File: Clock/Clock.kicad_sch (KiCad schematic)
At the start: 65 parts, among them J1 Conn buss, J10 Conn_buss, J11 Conn_buss, J12 Conn_buss, J13 Register_A-1,2 LED Conn, J14 Register_B-1,2 LED Conn, J15 Program Counter LED Conn, J16 Memory Address Reg LED Conn, J17 Instruction Reg LED Conn, J18 Conn_01x02_Pin, J19 Conn_02x04_Top_Bottom, J2 USB4125-GF-A, J3 Fuse-Block, J4 Conn buss, J5 Conn_buss, J6 Conn_buss, J7 Conn_buss, J8 Conn_buss, J9 Conn_buss, SW1 SW_CLK_mono, SW2 SW_Select_Mon/Ast, SW3 SW_SPST, SW4 SW_Select_Oscilator, U1 NE555P, U10 CD74HCT153E, U2 NE555P, U3 NE555P, U4 74LS04, U5 74LS08, U6 CD74HCT14E, U7 NE555P, U9 74HCT244, Y1 ECS-100AX-010

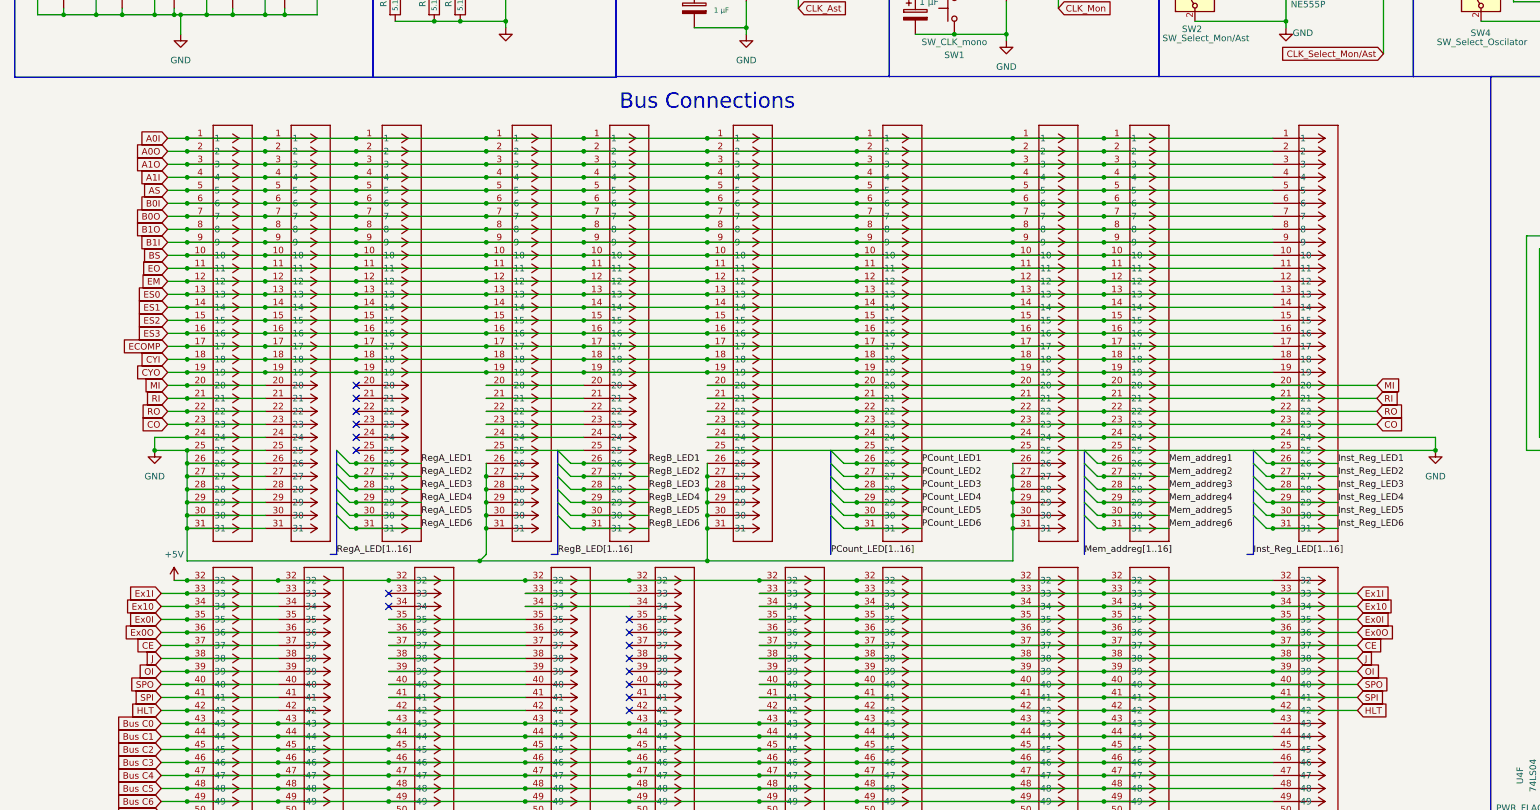
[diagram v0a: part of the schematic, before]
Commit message: Changed backplane signal layout, connected data bus
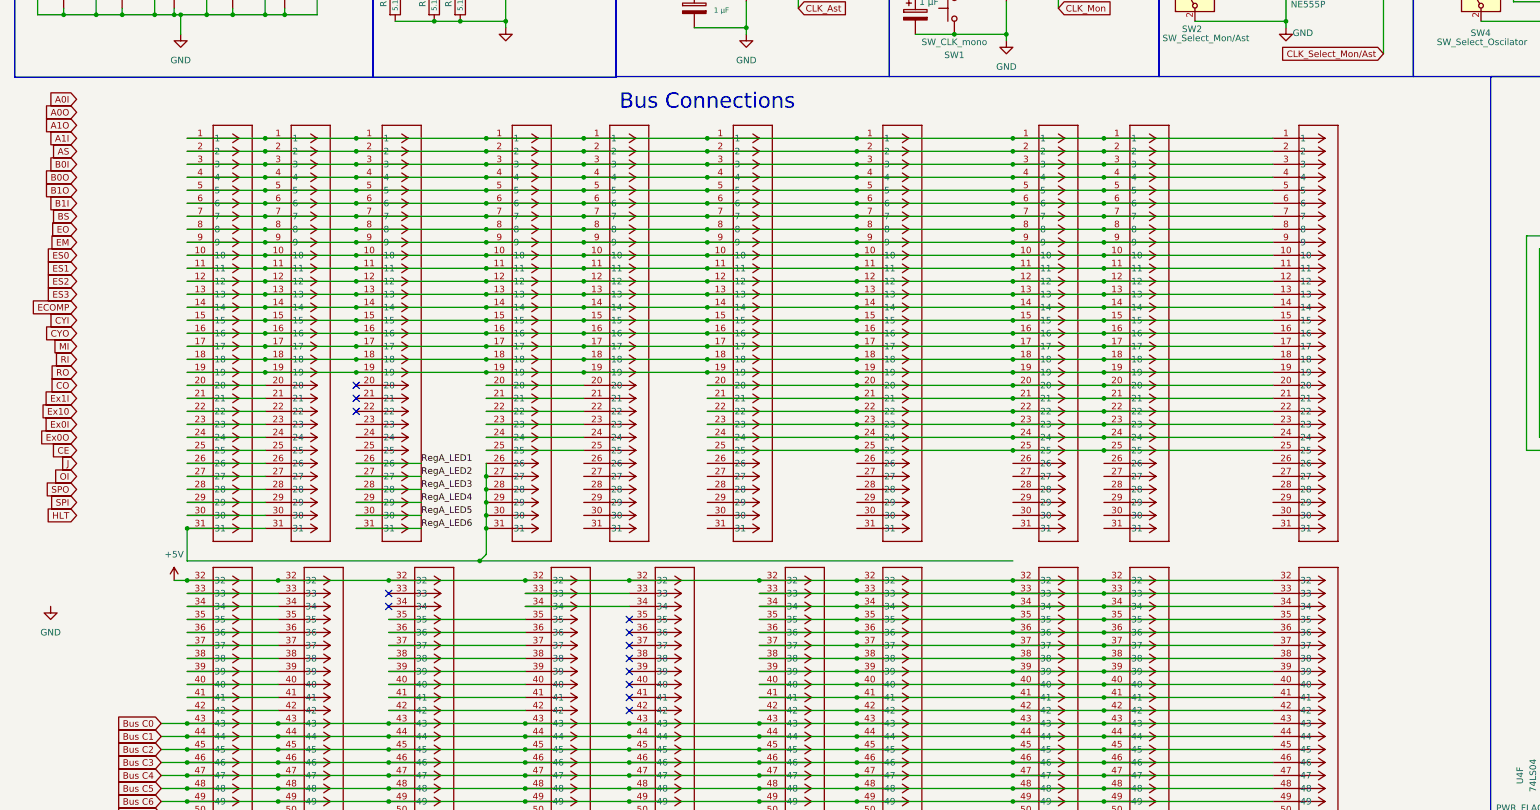
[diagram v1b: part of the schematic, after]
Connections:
- net A0I: no longer J1.1, J10.1, J11.1, J12.1, J4.1, J5.1, J6.1, J7.1, J8.1, J9.1
- net A0O: no longer J1.2, J10.2, J11.2, J12.2, J4.2, J5.2, J6.2, J7.2, J8.2, J9.2
- net A1I: no longer J1.4, J10.4, J11.4, J12.4, J4.4, J5.4, J6.4, J7.4, J8.4, J9.4
- net A1O: no longer J1.3, J10.3, J11.3, J12.3, J4.3, J5.3, J6.3, J7.3, J8.3, J9.3
- net AS: no longer J1.5, J10.5, J11.5, J12.5, J4.5, J5.5, J6.5, J7.5, J8.5, J9.5
- net B0I: no longer J1.6, J10.6, J11.6, J12.6, J4.6, J5.6, J6.6, J7.6, J8.6, J9.6
- net B0O: no longer J1.7, J10.7, J11.7, J12.7, J4.7, J5.7, J6.7, J7.7, J8.7, J9.7
- net B1I: no longer J1.9, J10.9, J11.9, J12.9, J4.9, J5.9, J6.9, J7.9, J8.9, J9.9
- net B1O: no longer J1.8, J10.8, J11.8, J12.8, J4.8, J5.8, J6.8, J7.8, J8.8, J9.8
- net BS: no longer J1.10, J10.10, J11.10, J12.10, J4.10, J5.10, J6.10, J7.10, J8.10, J9.10
- net CE: no longer J1.37, J10.37, J12.37, J4.37, J5.37, J6.37, J8.37
- net CO: no longer J1.23, J10.23, J12.23, J4.23, J5.23, J6.23, J8.23
- net CYI: no longer J1.18, J10.18, J11.18, J12.18, J4.18, J5.18, J6.18, J7.18, J8.18, J9.18
- net CYO: no longer J1.19, J10.19, J11.19, J12.19, J4.19, J5.19, J6.19, J7.19, J8.19, J9.19
- net ECOMP: no longer J1.17, J10.17, J11.17, J12.17, J4.17, J5.17, J6.17, J7.17, J8.17, J9.17
- net EM: no longer J1.12, J10.12, J11.12, J12.12, J4.12, J5.12, J6.12, J7.12, J8.12, J9.12
- net EO: no longer J1.11, J10.11, J11.11, J12.11, J4.11, J5.11, J6.11, J7.11, J8.11, J9.11
- net ES0: no longer J1.13, J10.13, J11.13, J12.13, J4.13, J5.13, J6.13, J7.13, J8.13, J9.13
- net ES1: no longer J1.14, J10.14, J11.14, J12.14, J4.14, J5.14, J6.14, J7.14, J8.14, J9.14
- net ES2: no longer J1.15, J10.15, J11.15, J12.15, J4.15, J5.15, J6.15, J7.15, J8.15, J9.15
- net ES3: no longer J1.16, J10.16, J11.16, J12.16, J4.16, J5.16, J6.16, J7.16, J8.16, J9.16
- net Ex0I: no longer J1.35, J10.35, J12.35, J4.35, J5.35, J6.35, J8.35
- net Ex0O: no longer J1.36, J10.36, J12.36, J4.36, J5.36, J6.36, J8.36
- net Ex10: no longer J1.34, J10.34, J12.34, J4.34, J5.34, J6.34, J8.34
- net Ex1I: no longer J1.33, J10.33, J12.33, J4.33, J5.33, J6.33, J8.33
- net GND: no longer J1.24, J1.25, J10.24, J10.25, J10.26, J10.27, J10.28, J10.29, J10.30, J10.31, J12.24, J12.25, J12.26, J12.27, J12.28, J12.29, J12.30, J12.31, J4.24, J4.25, J4.26, J4.27, J4.28, J4.29, J4.30, J4.31, J5.24, J5.25, J6.24, J6.25, J6.26, J6.27, J6.28, J6.29, J6.30, J6.31, J7.26, J7.27, J7.28, J7.29, J7.30, J7.31, J8.24, J8.25
- net HLT: no longer J1.42, J10.42, J12.42, J4.42, J5.42, J6.42, J8.42
- net Inst_Reg_LED1: no longer J1.26
- net Inst_Reg_LED2: no longer J1.27
- net Inst_Reg_LED3: no longer J1.28
- net Inst_Reg_LED4: no longer J1.29
- net Inst_Reg_LED5: no longer J1.30
- net Inst_Reg_LED6: no longer J1.31
- net J: no longer J1.38, J10.38, J12.38, J4.38, J5.38, J6.38, J8.38
- net MI: no longer J1.20, J10.20, J12.20, J4.20, J5.20, J6.20, J8.20
- net Mem_addreg1: no longer J5.26
- net Mem_addreg2: no longer J5.27
- net Mem_addreg3: no longer J5.28
- net Mem_addreg4: no longer J5.29
- net Mem_addreg5: no longer J5.30
- net Mem_addreg6: no longer J5.31
- net OI: no longer J1.39, J10.39, J12.39, J4.39, J5.39, J6.39, J8.39
- net PCount_LED1: no longer J8.26
- net PCount_LED2: no longer J8.27
- net PCount_LED3: no longer J8.28
- net PCount_LED4: no longer J8.29
- net PCount_LED5: no longer J8.30
- net PCount_LED6: no longer J8.31
- net RI: no longer J1.21, J10.21, J12.21, J4.21, J5.21, J6.21, J8.21
- net RO: no longer J1.22, J10.22, J12.22, J4.22, J5.22, J6.22, J8.22
- net RegB_LED1: no longer J9.26
- net RegB_LED2: no longer J9.27
- net RegB_LED3: no longer J9.28
- net RegB_LED4: no longer J9.29
- net RegB_LED5: no longer J9.30
- net RegB_LED6: no longer J9.31
- net SPI: no longer J1.41, J10.41, J12.41, J4.41, J5.41, J6.41, J8.41
- net SPO: no longer J1.40, J10.40, J12.40, J4.40, J5.40, J6.40, J8.40
- new net: J1.1, J10.1, J11.1, J12.1, J4.1, J5.1, J6.1, J7.1, J8.1, J9.1
- new net: J1.10, J10.10, J11.10, J12.10, J4.10, J5.10, J6.10, J7.10, J8.10, J9.10
- new net: J1.11, J10.11, J11.11, J12.11, J4.11, J5.11, J6.11, J7.11, J8.11, J9.11
- new net: J1.12, J10.12, J11.12, J12.12, J4.12, J5.12, J6.12, J7.12, J8.12, J9.12
- new net: J1.13, J10.13, J11.13, J12.13, J4.13, J5.13, J6.13, J7.13, J8.13, J9.13
- new net: J1.14, J10.14, J11.14, J12.14, J4.14, J5.14, J6.14, J7.14, J8.14, J9.14
- new net: J1.15, J10.15, J11.15, J12.15, J4.15, J5.15, J6.15, J7.15, J8.15, J9.15
- new net: J1.16, J10.16, J11.16, J12.16, J4.16, J5.16, J6.16, J7.16, J8.16, J9.16
- new net: J1.17, J10.17, J11.17, J12.17, J4.17, J5.17, J6.17, J7.17, J8.17, J9.17
- new net: J1.18, J10.18, J11.18, J12.18, J4.18, J5.18, J6.18, J7.18, J8.18, J9.18
- new net: J1.19, J10.19, J11.19, J12.19, J4.19, J5.19, J6.19, J7.19, J8.19, J9.19
- new net: J1.2, J10.2, J11.2, J12.2, J4.2, J5.2, J6.2, J7.2, J8.2, J9.2
- new net: J10.31, J12.31, J7.26, J7.27, J7.28, J7.29, J7.30, J7.31
- new net: J1.3, J10.3, J11.3, J12.3, J4.3, J5.3, J6.3, J7.3, J8.3, J9.3
- new net: J1.4, J10.4, J11.4, J12.4, J4.4, J5.4, J6.4, J7.4, J8.4, J9.4
- new net: J1.5, J10.5, J11.5, J12.5, J4.5, J5.5, J6.5, J7.5, J8.5, J9.5
- new net: J1.6, J10.6, J11.6, J12.6, J4.6, J5.6, J6.6, J7.6, J8.6, J9.6
- new net: J1.7, J10.7, J11.7, J12.7, J4.7, J5.7, J6.7, J7.7, J8.7, J9.7
- new net: J1.8, J10.8, J11.8, J12.8, J4.8, J5.8, J6.8, J7.8, J8.8, J9.8
- new net: J1.9, J10.9, J11.9, J12.9, J4.9, J5.9, J6.9, J7.9, J8.9, J9.9
- new net: J10.20, J12.20
- new net: J10.21, J12.21
- new net: J10.22, J12.22
- new net: J10.23, J12.23
- new net: J10.24, J12.24
- new net: J10.25, J12.25
- new net: J10.26, J12.26
- new net: J10.27, J12.27
- new net: J10.28, J12.28
- new net: J10.29, J12.29
- new net: J10.30, J12.30
- new net: J1.20, J4.20, J5.20, J6.20, J8.20
- new net: J1.21, J4.21, J5.21, J6.21, J8.21
- new net: J1.22, J4.22, J5.22, J6.22, J8.22
- new net: J1.23, J4.23, J5.23, J6.23, J8.23
- new net: J1.24, J4.24, J5.24, J6.24, J8.24
- new net: J1.25, J4.25, J5.25, J6.25, J8.25
- new net: J1.33, J4.33, J5.33, J6.33, J8.33
- new net: J1.34, J4.34, J5.34, J6.34, J8.34
- new net: J1.35, J4.35, J5.35, J6.35, J8.35
- new net: J1.36, J4.36, J5.36, J6.36, J8.36
- new net: J1.37, J4.37, J5.37, J6.37, J8.37
- new net: J1.38, J4.38, J5.38, J6.38, J8.38
- new net: J1.39, J4.39, J5.39, J6.39, J8.39
- new net: J1.40, J4.40, J5.40, J6.40, J8.40
- new net: J1.41, J4.41, J5.41, J6.41, J8.41
- new net: J1.42, J4.42, J5.42, J6.42, J8.42
- new net: J10.33, J12.33
- new net: J10.34, J12.34
- new net: J10.35, J12.35
- new net: J10.36, J12.36
- new net: J10.37, J12.37
- new net: J10.38, J12.38
- new net: J10.39, J12.39
- new net: J10.40, J12.40
- new net: J10.41, J12.41
- new net: J10.42, J12.42
- no-connect marks 90 -> 87
